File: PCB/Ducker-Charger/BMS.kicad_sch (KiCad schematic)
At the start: 44 parts, among them IC3 BQ34Z100PWR-R2, Q1 BSC040N08NS5, Q12 BC846, Q2 BSC040N08NS5, U8 BQ7791500PWR, U9 ISO1540DR

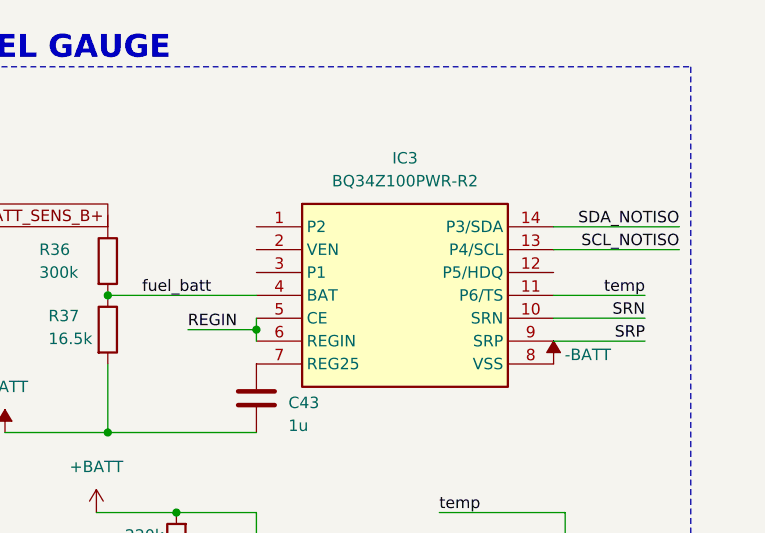
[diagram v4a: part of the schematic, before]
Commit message: fix: changed rshunt footprint
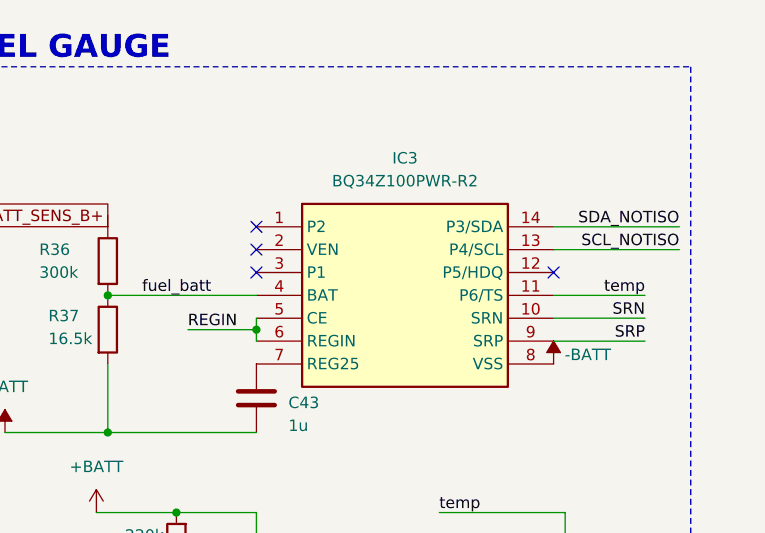
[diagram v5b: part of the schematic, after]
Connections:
- no-connect marks 2 -> 6
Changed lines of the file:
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@@
+	)
+	(no_connect
+		(at 267.97 54.61)
+	)
+	(no_connect
+		(at 234.95 54.61)
 	)
 	(no_connect
@@
 		(at 156.21 64.77)
 	)
+	(no_connect
+		(at 234.95 52.07)
+	)
+	(no_connect
+		(at 234.95 49.53)
+	)
 	(bus_entry

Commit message: feat: remade the PCB & minor schematic fixes
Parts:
- D501: renamed from D3; value D_Zener -> 5V
- R515: renamed from R40; value 220k -> 15k
- RDSG501: renamed from RDSG1; value 4k5 -> 1k
- renumbered C44 to C501, C45 to C502, C46 to C503, C48 to C504, C49 to C505, C50 to C506, C55 to C507, C54 to C508, C43 to C509, C47 to C510, C_VDD1 to C_VDD501, C_VDD2 to C_VDD502, IC3 to IC501, Q1 to Q501, Q2 to Q502, Q12 to Q503, R47 to R501, R38 to R502, R39 to R503, R41 to R504, R44 to R505, R45 to R506, R48 to R507, R42 to R508, R43 to R509, R46 to R510, R35 to R511, R36 to R512, R37 to R513, R56 to R514, R55 to R516, RCHG1 to RCHG501, RGS1 to RGS501, RGS2 to RGS502, RLD1 to RLD501, RSNS2 to RSNS501, R_VDD1 to R_VDD501, TH2 to TH501, TH1 to TH502, U8 to U501, U9 to U502
